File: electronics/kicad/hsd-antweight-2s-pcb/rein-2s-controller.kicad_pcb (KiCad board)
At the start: 2 copper layers, 46 x 67 mm, 11 parts, among them J10 3V3 GND VBAT_SW, J4 BATTERY, J5 MOTOR LEFT, J6 MOTOR RIGHT, J8 ESP32 LEFT ALL PINS, J9 ESP32 RIGHT SIGNALS, SW1 SW EXT VBAT_RAW/VBAT_SW, U1 ESP32-C3 SUPERMINI, U2 DRV8833, U3 EXT REG LOGIC VIN GND VOUT

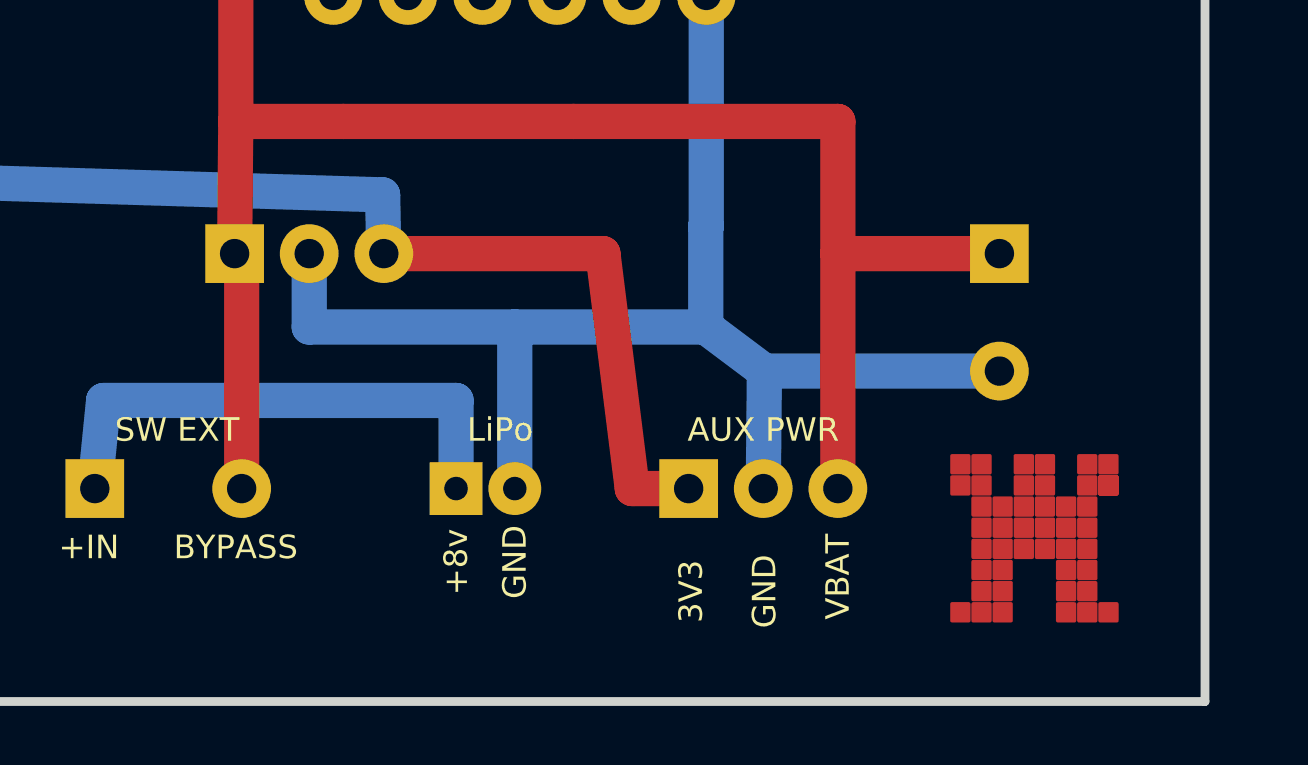
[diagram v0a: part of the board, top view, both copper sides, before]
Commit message: docs(kicad): refresh bare PCB renders and silk labels
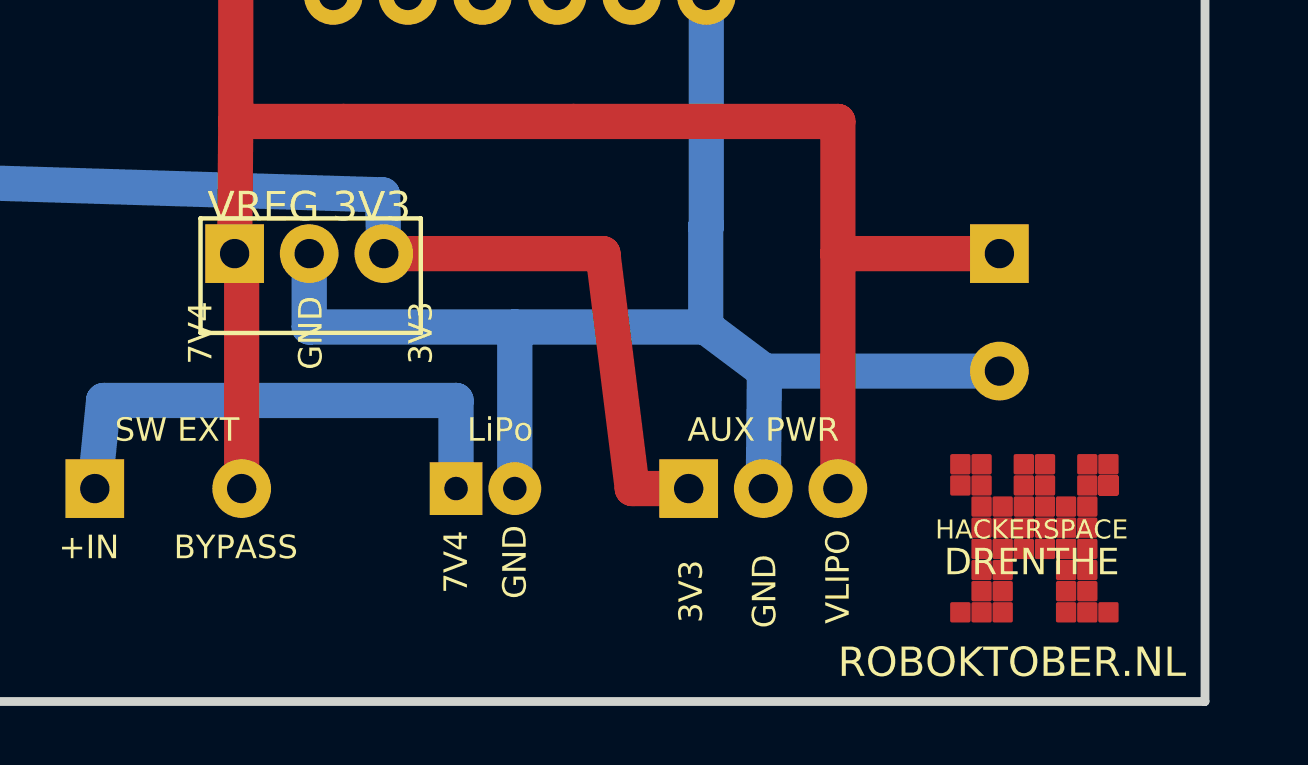
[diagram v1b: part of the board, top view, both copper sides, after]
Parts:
- J10: value 3V3 GND VBAT_SW -> 3V3 GND VLIPO
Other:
- board text added: "7V4"
- board text added: "DRENTHE"
- board text added: "HACKERSPACE"
- board text added: "ROBOKTOBER.NL"
- board text added: "VLIPO"
- board text added: "VREG 3V3"
- board text removed: "+8v"
- board text removed: "VBAT"
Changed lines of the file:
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@@
 			)
 		)
-		(property "Value" "3V3 GND VBAT_SW"
+		(property "Value" "3V3 GND VLIPO"
 			(at 2.54 3 0)
 			(layer "F.Fab")
@@
 	)
 	(gr_rect
+		(start 25.8 67.3)
+		(end 33.3 71.2)
+		(stroke
+			(width 0.15)
+			(type solid)
+		)
+		(fill no)
+		(layer "F.SilkS")
+	)
+	(gr_rect
 		(start 14.02 16.75)
 		(end 60 83.75)
@@
 		(layer "Edge.Cuts")
 	)
+	(gr_text "HACKERSPACE"
+		(at 54.1 77.9 0)
+		(layer "F.SilkS")
+		(effects
+			(font
+				(size 0.65 0.65)
+				(thickness 0.1)
+			)
+		)
+	)
 	(gr_text "M1A"
 		(at 18.5 52 0)
@@
 		)
 	)
+	(gr_text "7V4"
+		(at 25.8 71.2 90)
+		(layer "F.SilkS")
+		(effects
+			(font
+				(size 0.8 0.8)
+				(thickness 0.12)
+			)
+		)
+	)
+	(gr_text "GND"
+		(at 29.55 71.2 90)
+		(layer "F.SilkS")
+		(effects
+			(font
+				(size 0.8 0.8)
+				(thickness 0.12)
+			)
+		)
+	)
 	(gr_text "AI1"
 		(at 30.32 47.75 90)
@@
 		)
 	)
-	(gr_text "+8v"
+	(gr_text "3V3"
+		(at 33.3 71.2 90)
+		(layer "F.SilkS")
+		(effects
+			(font
+				(size 0.8 0.8)
+				(thickness 0.12)
+			)
+		)
+	)
+	(gr_text "7V4"
 		(at 34.5 79 90)
 		(layer "F.SilkS")
@@
 		)
 	)
-	(gr_text "VBAT"
+	(gr_text "VLIPO"
 		(at 47.5 79.5 90)
 		(layer "F.SilkS")
@@
 			)
 		)
+	)
+	(gr_text "DRENTHE"
+		(at 54.1 79 0)
+		(layer "F.SilkS")
+		(effects
+			(font
+				(size 0.9 0.9)
+				(thickness 0.12)
+			)
+		)
+	)
+	(gr_text "ROBOKTOBER.NL"
+		(at 47.5 83 0)
+		(layer "F.SilkS")
+		(effects
+			(font
+				(size 1 1)
+				(thickness 0.1)
+			)
+			(justify left bottom)
+		)
+	)
+	(gr_text "VREG 3V3"
+		(at 29.5 66.9 0)
+		(layer "F.SilkS")
+		(effects
+			(font
+				(size 1 1)
+				(thickness 0.15)
+			)
+		)
